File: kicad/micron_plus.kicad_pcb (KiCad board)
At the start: 2 copper layers, 163.8 x 123.2 mm, 82 parts, among them J1 Conn_02x17_Odd_Even, J2 Conn_01x01_Female, J3 Conn_01x01_Female, Q1 2N2905A, Q2 2N2905A, Q3 2N3904, Q4 2N3904, T1 Transformer_1P_2S, U1 MC68A21, U10 74LS00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

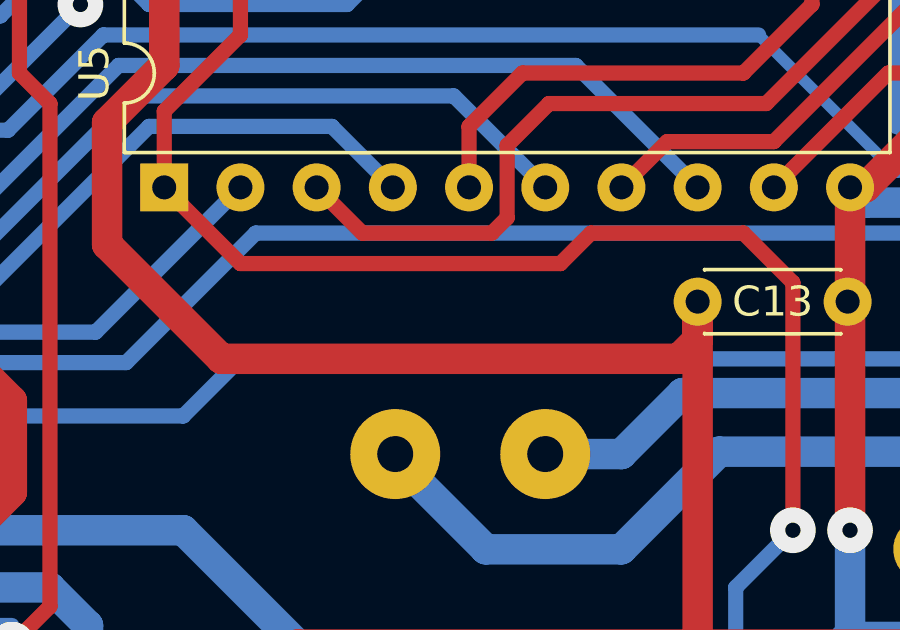
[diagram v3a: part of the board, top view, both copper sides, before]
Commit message: KiCAD: Added R19 (VCCEnable pullup)
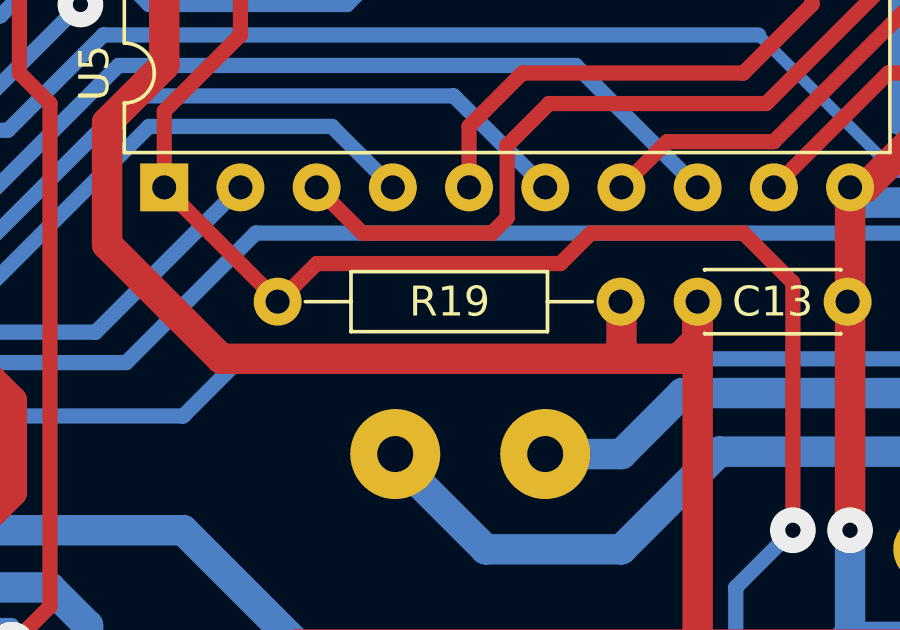
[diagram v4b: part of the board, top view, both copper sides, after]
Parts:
- added R19: 4K7, custom_footprints:R_Axial_DIN0207_L6.3mm_D2.0mm_P11.43mm_Horizontal, F.Cu at (147.3, 105.4)
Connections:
- net Net-(C9-Pad2) renamed /Power Supply/AC4
- net Net-(D4-Pad2) renamed /Power Supply/AC2
- net Net-(D4-Pad4) renamed /Power Supply/AC1
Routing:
- net VCC: track 894.9 -> 896.8 mm
- net /Control Latches/nVCCEnable: track 361.7 -> 362.8 mm

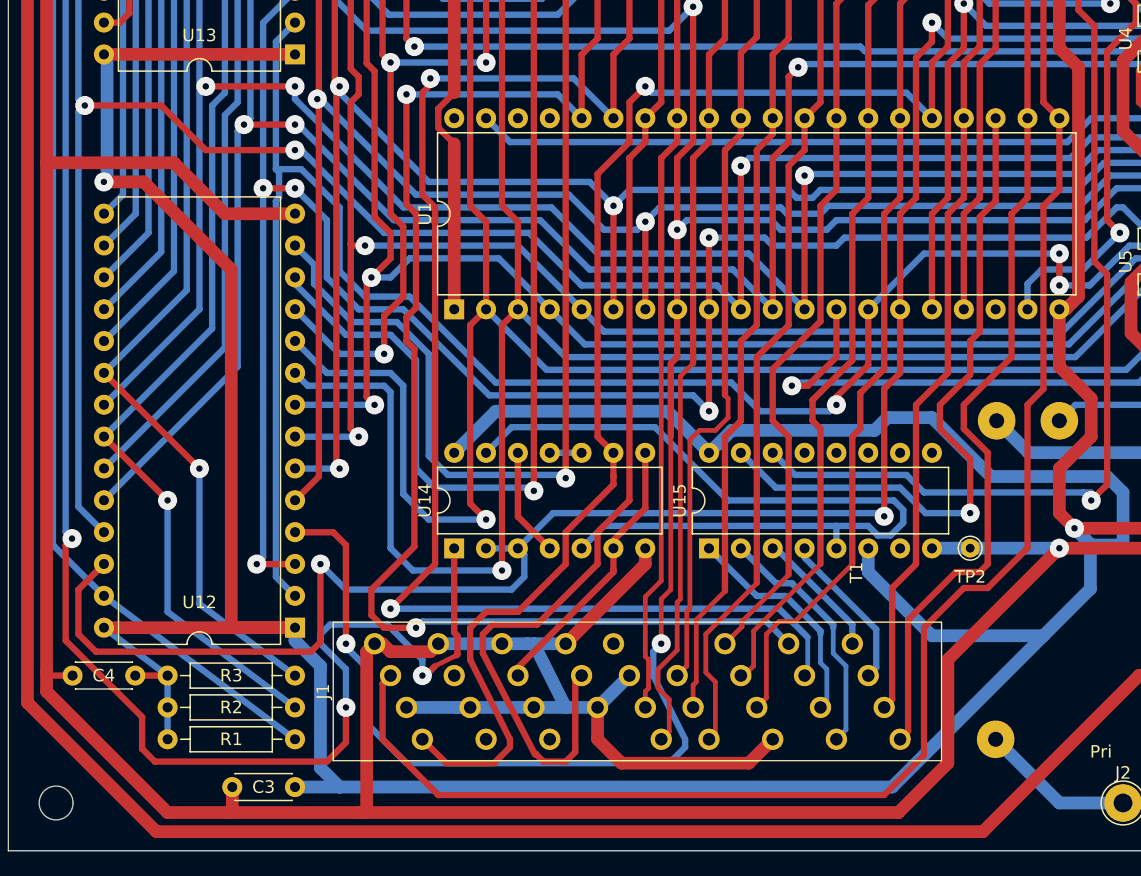
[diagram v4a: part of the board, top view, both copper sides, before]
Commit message: KiCAD: Replace transition header with normal pin header
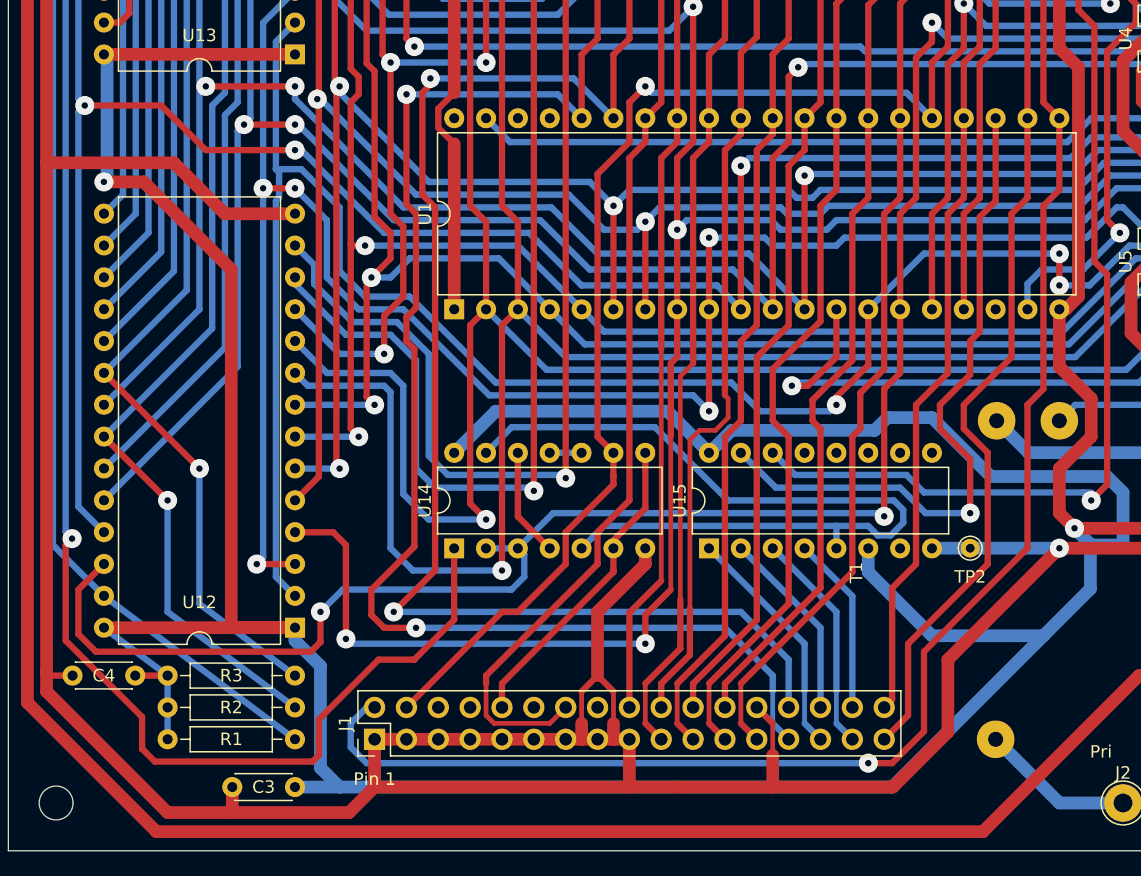
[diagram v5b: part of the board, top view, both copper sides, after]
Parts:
- J1: footprint custom_footprints:TransitionHeader_34_P2.54mm_Vertical -> Connector_PinHeader_2.54mm:PinHeader_2x17_P2.54mm_Vertical
- moved J1 7.62 mm to (69.8, 135.9)
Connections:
- U1 pad 22: /1MHz Bus and PIA Interface/bus_A7 -> /1MHz Bus and PIA Interface/bus_A6
- U1 pad 24: /1MHz Bus and PIA Interface/bus_A6 -> /1MHz Bus and PIA Interface/bus_A7
- U2 pad 22: /1MHz Bus and PIA Interface/bus_A7 -> /1MHz Bus and PIA Interface/bus_A6
- U2 pad 24: /1MHz Bus and PIA Interface/bus_A6 -> /1MHz Bus and PIA Interface/bus_A7
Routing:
- net GND: track 974.4 -> 946.7 mm
- net /1MHz Bus and PIA Interface/Addr6: track 196.2 -> 176.9 mm
- net /Buffer RAM/nAddr13: track 119.3 -> 107.1 mm, vias 4 -> 2
- net /1MHz Bus and PIA Interface/bus_1MHzE: track 123.0 -> 112.1 mm
- net /1MHz Bus and PIA Interface/bus_nRST: track 98.3 -> 89.0 mm
- net /1MHz Bus and PIA Interface/bus_D5: track 75.6 -> 84.3 mm
- net /1MHz Bus and PIA Interface/bus_A4: track 10.1 -> 17.8 mm
- net /1MHz Bus and PIA Interface/bus_A7: track 85.4 -> 78.6 mm
- net /1MHz Bus and PIA Interface/bus_A6: track 78.6 -> 84.8 mm
- net /1MHz Bus and PIA Interface/bus_A0: track 122.2 -> 127.2 mm
- net /1MHz Bus and PIA Interface/bus_A3: track 19.8 -> 15.3 mm
- net /1MHz Bus and PIA Interface/Addr13: track 164.5 -> 160.6 mm
- net /1MHz Bus and PIA Interface/bus_D3: track 78.6 -> 82.2 mm
- net /1MHz Bus and PIA Interface/bus_D6: track 78.1 -> 81.2 mm
- net /1MHz Bus and PIA Interface/bus_RnW: track 137.1 -> 134.0 mm, vias 0 -> 1
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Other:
- board text added: "Pin 1"

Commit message: KiCAD: Replace transformer with DC Jack + Boost Converter
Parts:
- removed the C9 at (162.6, 137.2)
- removed D8, D9: 1N4001, custom_footprints:D_DO-41_SOD81_P11.43mm_Horizontal
- removed J3: Conn_01x01_Female, TestPoint:TestPoint_THTPad_D3.0mm_Drill1.5mm
- removed T1: Transformer_1P_2S, custom_footprints:Transformer_drake_p0609
- removed TP1, TP2: TestPoint, TestPoint:TestPoint_THTPad_D1.5mm_Drill0.7mm
- added C11: 100u/50V, Capacitor_THT:CP_Radial_D8.0mm_P5.00mm, F.Cu at (135.2, 132.7)
- added C12: 470p, Capacitor_THT:C_Disc_D4.3mm_W1.9mm_P5.00mm, F.Cu at (146.5, 117.5)
- added C14: 100n, Capacitor_THT:C_Disc_D4.3mm_W1.9mm_P5.00mm, F.Cu at (177.8, 111.8)
- added C7: 100n, Capacitor_THT:C_Disc_D4.3mm_W1.9mm_P5.00mm, F.Cu at (192.4, 133.3)
- added L1: 220uH, Inductor_THT:L_Radial_D14.2mm_P10.00mm_Neosid_SD14, F.Cu at (155.6, 123.8)
- added R20: 0R33, custom_footprints:R_Axial_DIN0207_L6.3mm_D2.0mm_P10.16mm_Horizontal, F.Cu at (141.5, 131.4)
- added R21: 180, custom_footprints:R_Axial_DIN0207_L6.3mm_D2.0mm_P10.16mm_Horizontal, F.Cu at (151.7, 135.3)
- added R22: 12K, custom_footprints:R_Axial_DIN0207_L6.3mm_D2.0mm_P10.16mm_Horizontal, F.Cu at (132.6, 128.9)
- added R23: 560, custom_footprints:R_Axial_DIN0207_L6.3mm_D2.0mm_P10.16mm_Horizontal, F.Cu at (137.7, 118.7)
- added R24: 5K6, Resistor_THT:R_Axial_DIN0207_L6.3mm_D2.5mm_P10.16mm_Horizontal, F.Cu at (189.2, 115.6)
- added U16: MC34063AP, Package_DIP:DIP-8_W7.62mm, F.Cu at (149.1, 120.0)
- C1: value 2200u/16V -> 330n; footprint Capacitor_THT:CP_Radial_D13.0mm_P5.00mm -> Capacitor_THT:C_Disc_D4.3mm_W1.9mm_P5.00mm
- C13: renamed from C10; value 220u/63V -> 100u/50V; footprint Capacitor_THT:CP_Radial_D10.0mm_P5.00mm -> Capacitor_THT:CP_Radial_D8.0mm_P5.00mm
- D4: value W005 -> 1N5819; footprint Diode_THT:Diode_Bridge_Round_D9.0mm -> Diode_THT:D_DO-41_SOD81_P10.16mm_Horizontal
- J2: value Conn_01x01_Female -> Cliff DC10A; footprint TestPoint:TestPoint_THTPad_D3.0mm_Drill1.5mm -> custom_footprints:CLIFF_FC68148(DC-10A)
- R5: footprint custom_footprints:R_Axial_DIN0207_L6.3mm_D2.0mm_P11.43mm_Horizontal -> custom_footprints:R_Axial_DIN0207_L6.3mm_D2.0mm_P10.16mm_Horizontal
- U20: value LM317L_TO92 -> LM317SP_TO220; footprint Package_TO_SOT_THT:TO-92_Inline_Wide -> Package_TO_SOT_THT:TO-220-3_Vertical
- moved C13 33.2 mm to (135.2, 114.9), turned to 90 degrees
- moved R5 24.1 mm to (174.0, 118.1), turned to -90 degrees
- moved D4 20.3 mm to (141.5, 113.7)
- moved C1 16.1 mm to (187.3, 133.3)
- moved C8 15.3 mm to (196.8, 120.0), turned to 90 degrees
- moved C9 13.1 mm to (190.5, 123.8)
- moved J2 7.65 mm to (121.9, 140.3)
- moved C10 1.82 mm to (191.8, 108.0)
- moved U20 0.64 mm to (173.4, 106.7)
- renumbered C8 to C10, C11 to C15, C12 to C16, C13 to C6, C6 to C8, C7 to C9
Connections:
- C1 pad 1: /Power Supply/10VDC -> /Power Supply/9VDC
- D10 pad 1: Net-(D10-Pad1) -> GND
- D10 pad 2: VCC -> Net-(D10-Pad2)
- D4 pad 1: /Power Supply/10VDC -> /Power Supply/28VDC
- D4 pad 2: /Power Supply/AC2 -> Net-(D4-Pad2)
- J2 pad 1: Net-(J2-Pad1) -> /Power Supply/9VDC
- R5 pad 1: Net-(D10-Pad1) -> VCC
- R5 pad 2: GND -> Net-(D10-Pad2)
- U18 pad 1: /Power Supply/10VDC -> /Power Supply/9VDC
- U19 pad 3: /Power Supply/10VDC -> /Power Supply/9VDC
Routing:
- net /Power Supply/10VDC: track 147.5 -> 0.00 mm, vias 1 -> 0
- net /Power Supply/9VDC: track 0.00 -> 115.5 mm
- net /Power Supply/AC4: track 71.2 -> 0.00 mm
- net VCC: track 896.8 -> 836.4 mm, vias 12 -> 15
- net GND: track 946.7 -> 1000.8 mm, vias 7 -> 4
- net /Main Logic and Eprom Socket/EpromVCC: track 377.9 -> 416.2 mm, vias 4 -> 3
- net Net-(L1-Pad1): track 0.00 -> 29.9 mm
- net Net-(D4-Pad2): track 0.00 -> 24.4 mm
- net /Power Supply/AC2: track 23.1 -> 0.00 mm
- net /Power Supply/AC1: track 22.5 -> 0.00 mm
- net /Power Supply/28VDC: track 40.3 -> 62.1 mm
- net Net-(D10-Pad1): track 18.2 -> 0.00 mm
- net /Control Latches/nVCCEnable: track 362.8 -> 345.5 mm, vias 2 -> 1
- net Net-(C8-Pad1): track 49.1 -> 33.4 mm
- net Net-(C9-Pad1) (its old number): track 14.2 -> 0.00 mm
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- added copper zone on B.Cu, net GND
